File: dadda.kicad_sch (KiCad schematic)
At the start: 0 parts

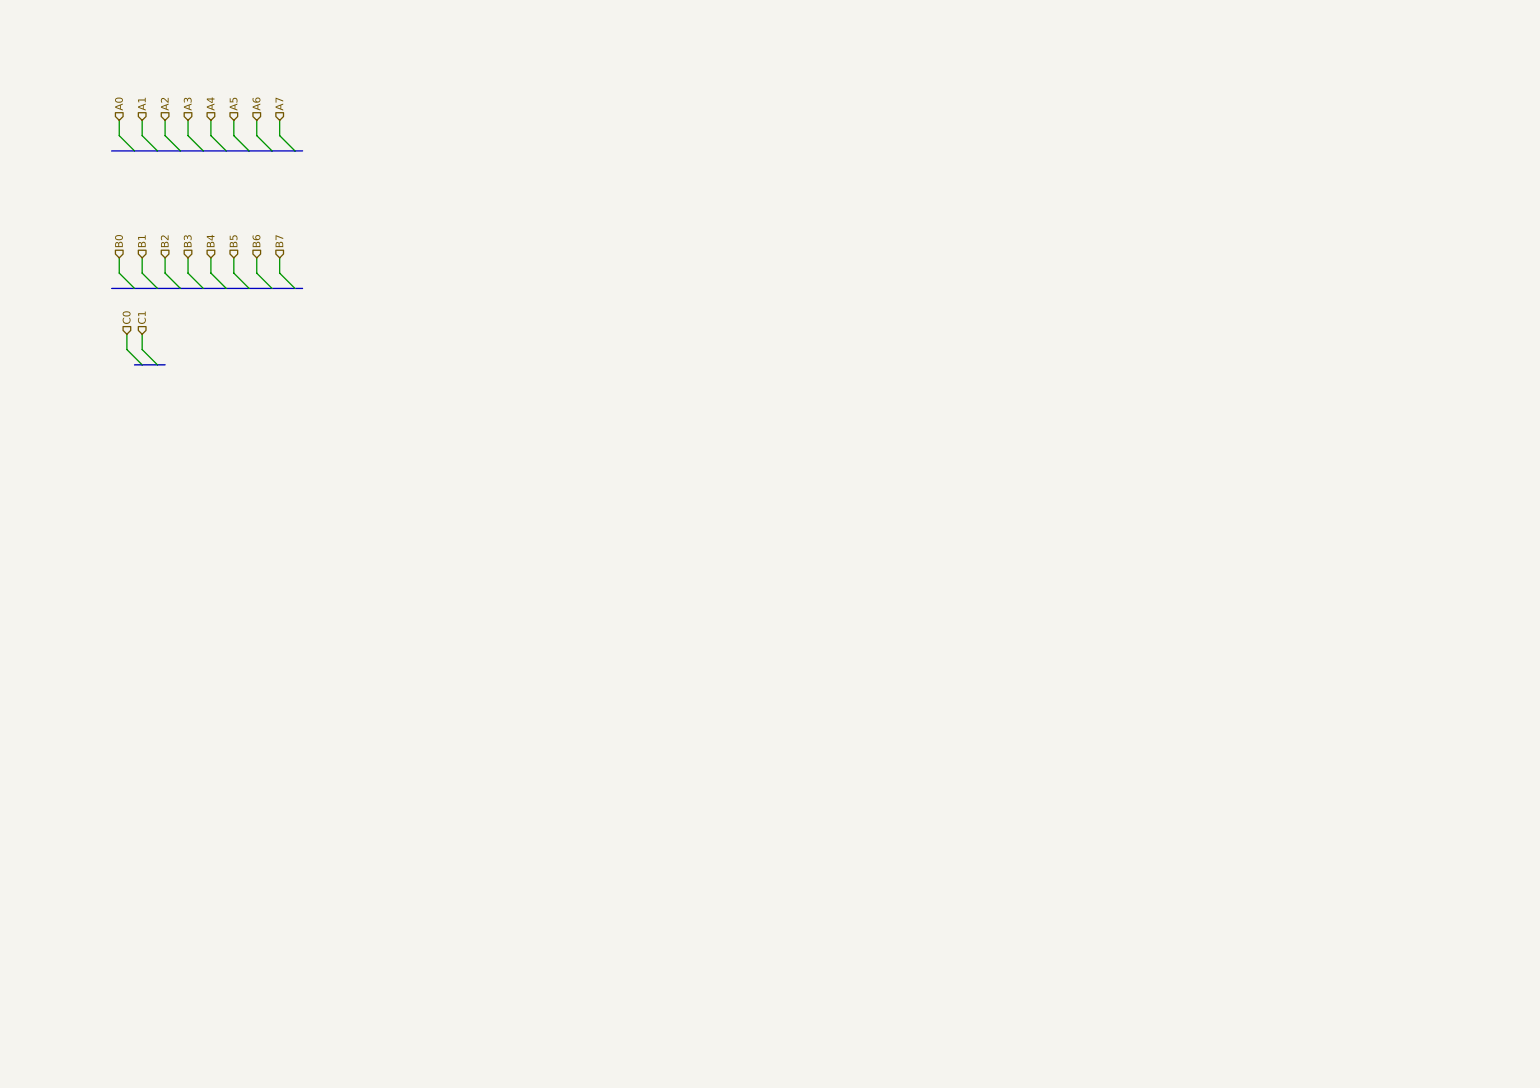
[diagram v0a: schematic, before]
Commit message: Added hierarchal partial product outputs, need to complete treemultiplier
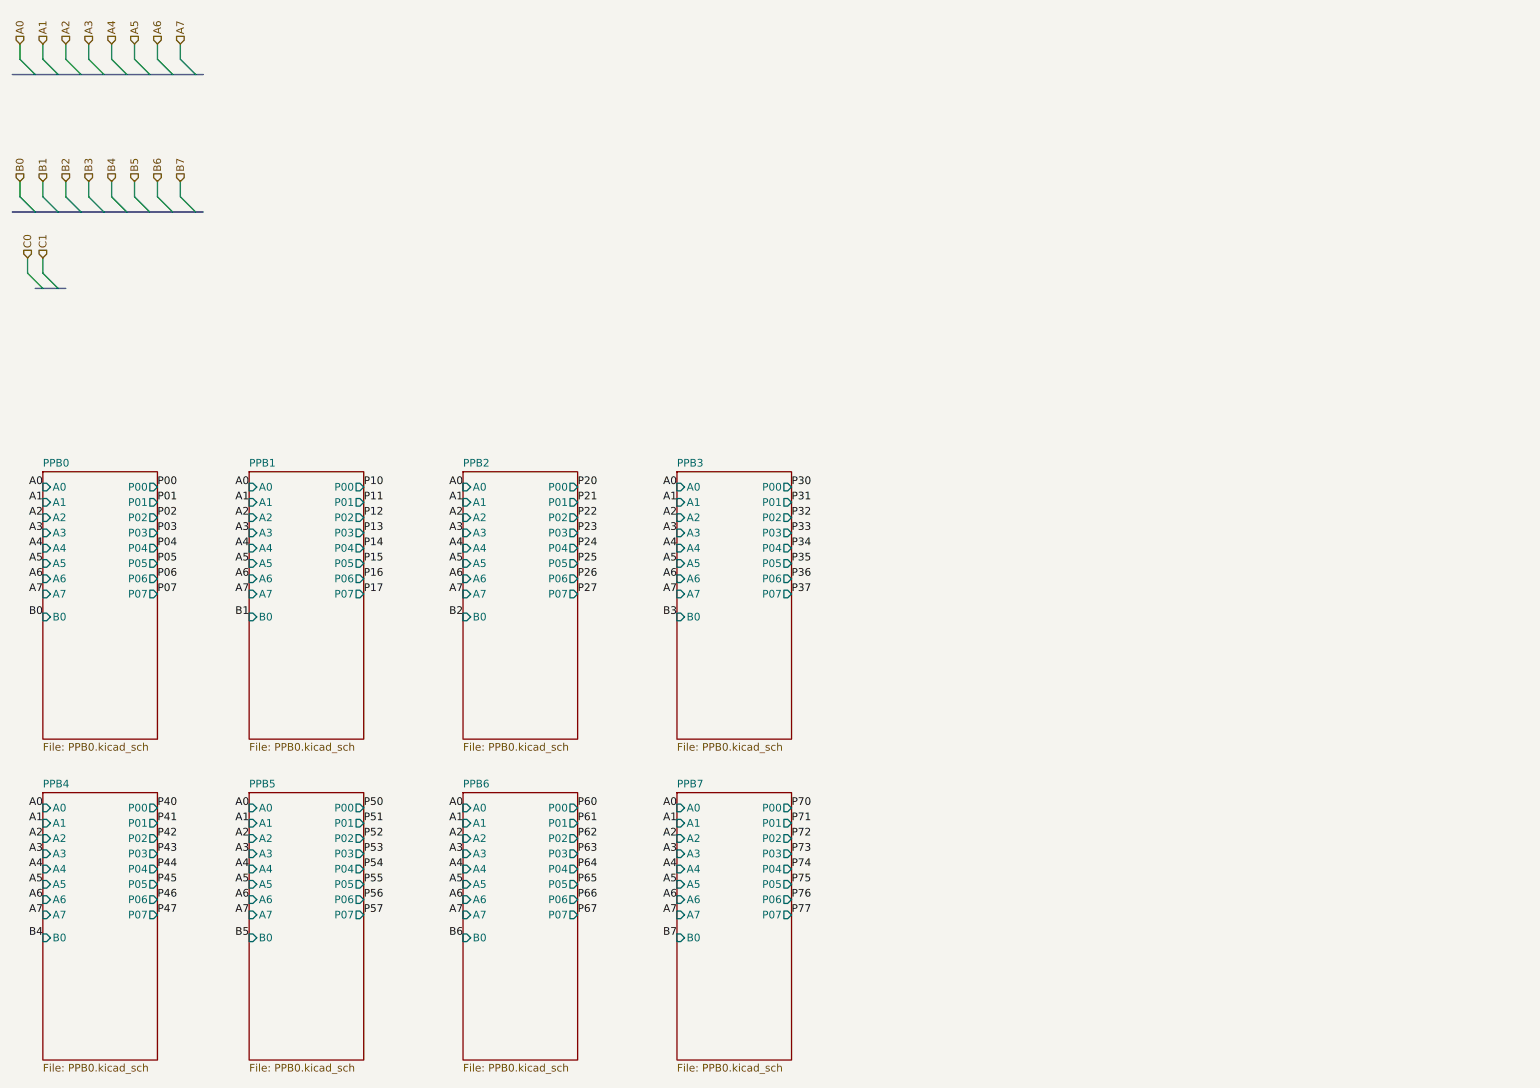
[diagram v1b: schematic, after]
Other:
- added sheet PPB0 (PPB0.kicad_sch)
- added sheet PPB1 (PPB0.kicad_sch)
- added sheet PPB2 (PPB0.kicad_sch)
- added sheet PPB3 (PPB0.kicad_sch)
- added sheet PPB4 (PPB0.kicad_sch)
- added sheet PPB5 (PPB0.kicad_sch)
- added sheet PPB6 (PPB0.kicad_sch)
- added sheet PPB7 (PPB0.kicad_sch)

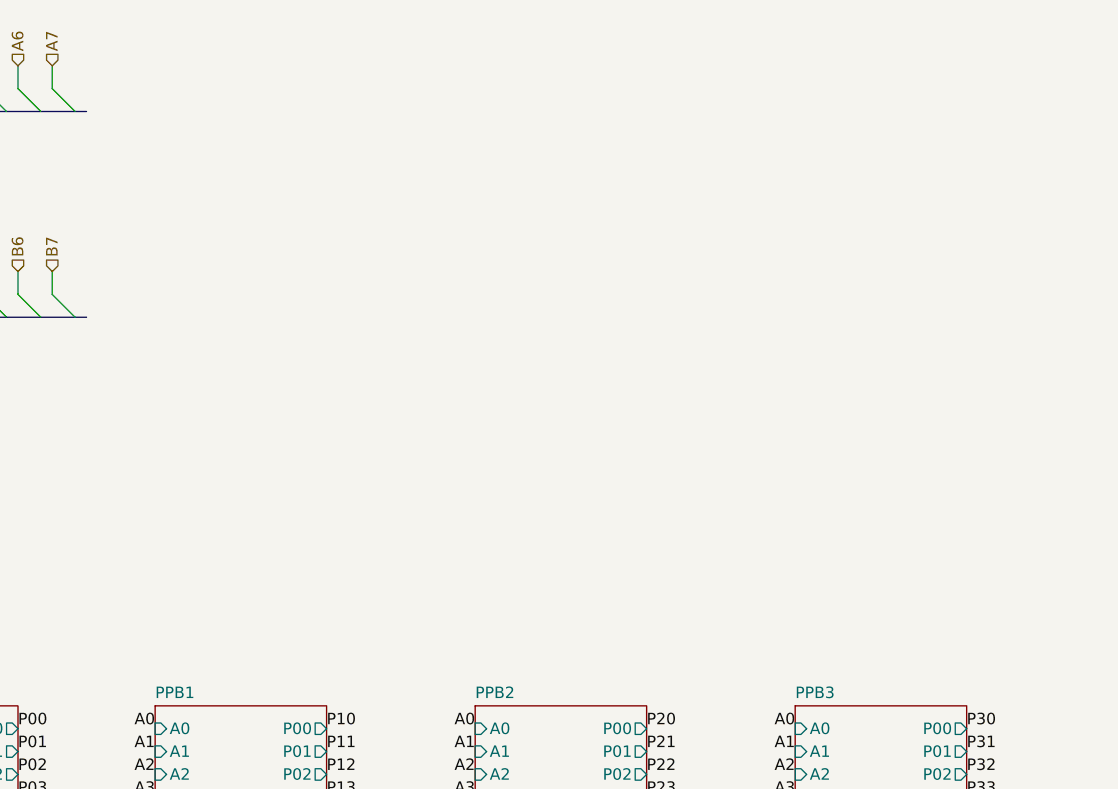
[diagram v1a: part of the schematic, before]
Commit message: Added first set of condensing adders, down to 4 rows total of Partials to add
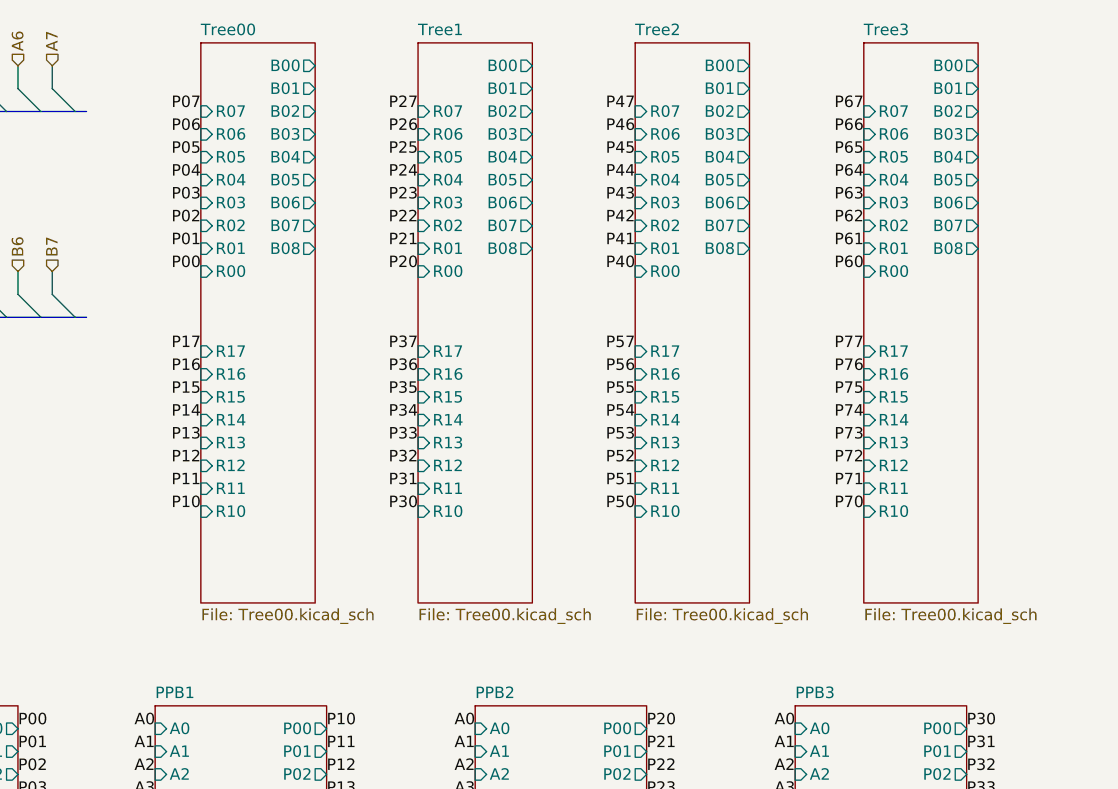
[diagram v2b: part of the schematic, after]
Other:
- added sheet Tree00 (Tree00.kicad_sch)
- added sheet Tree1 (Tree00.kicad_sch)
- added sheet Tree2 (Tree00.kicad_sch)
- added sheet Tree3 (Tree00.kicad_sch)

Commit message: Finished schematic, need to look at power output of the mux potentially to drive LED pins, otherwise logic SHOULD be done
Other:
- added sheet FinalTree (FinalTree.kicad_sch)
- added sheet Tree01 (Tree01.kicad_sch)
- added sheet Tree4 (Tree01.kicad_sch)
- sheet Tree00 ports: added B09; removed none
- sheet Tree1 ports: added B09; removed none
- sheet Tree2 ports: added B09; removed none
- sheet Tree3 ports: added B09; removed none

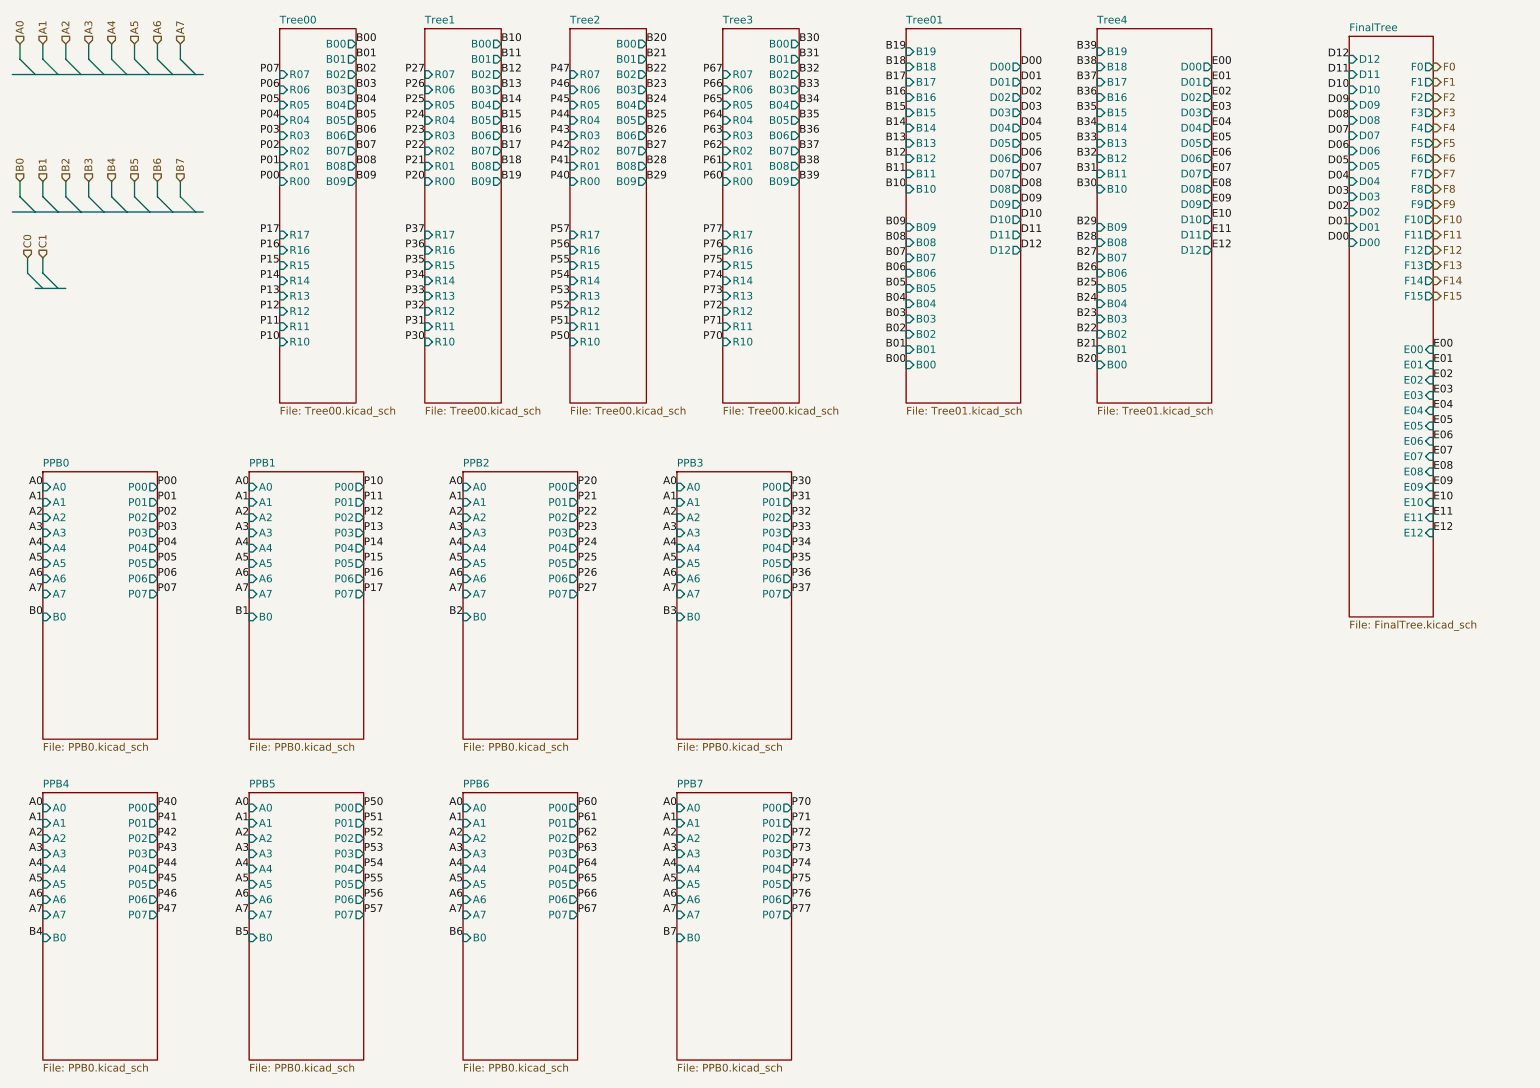
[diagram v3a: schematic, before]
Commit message: Fixed ERC issues and applied Footprints
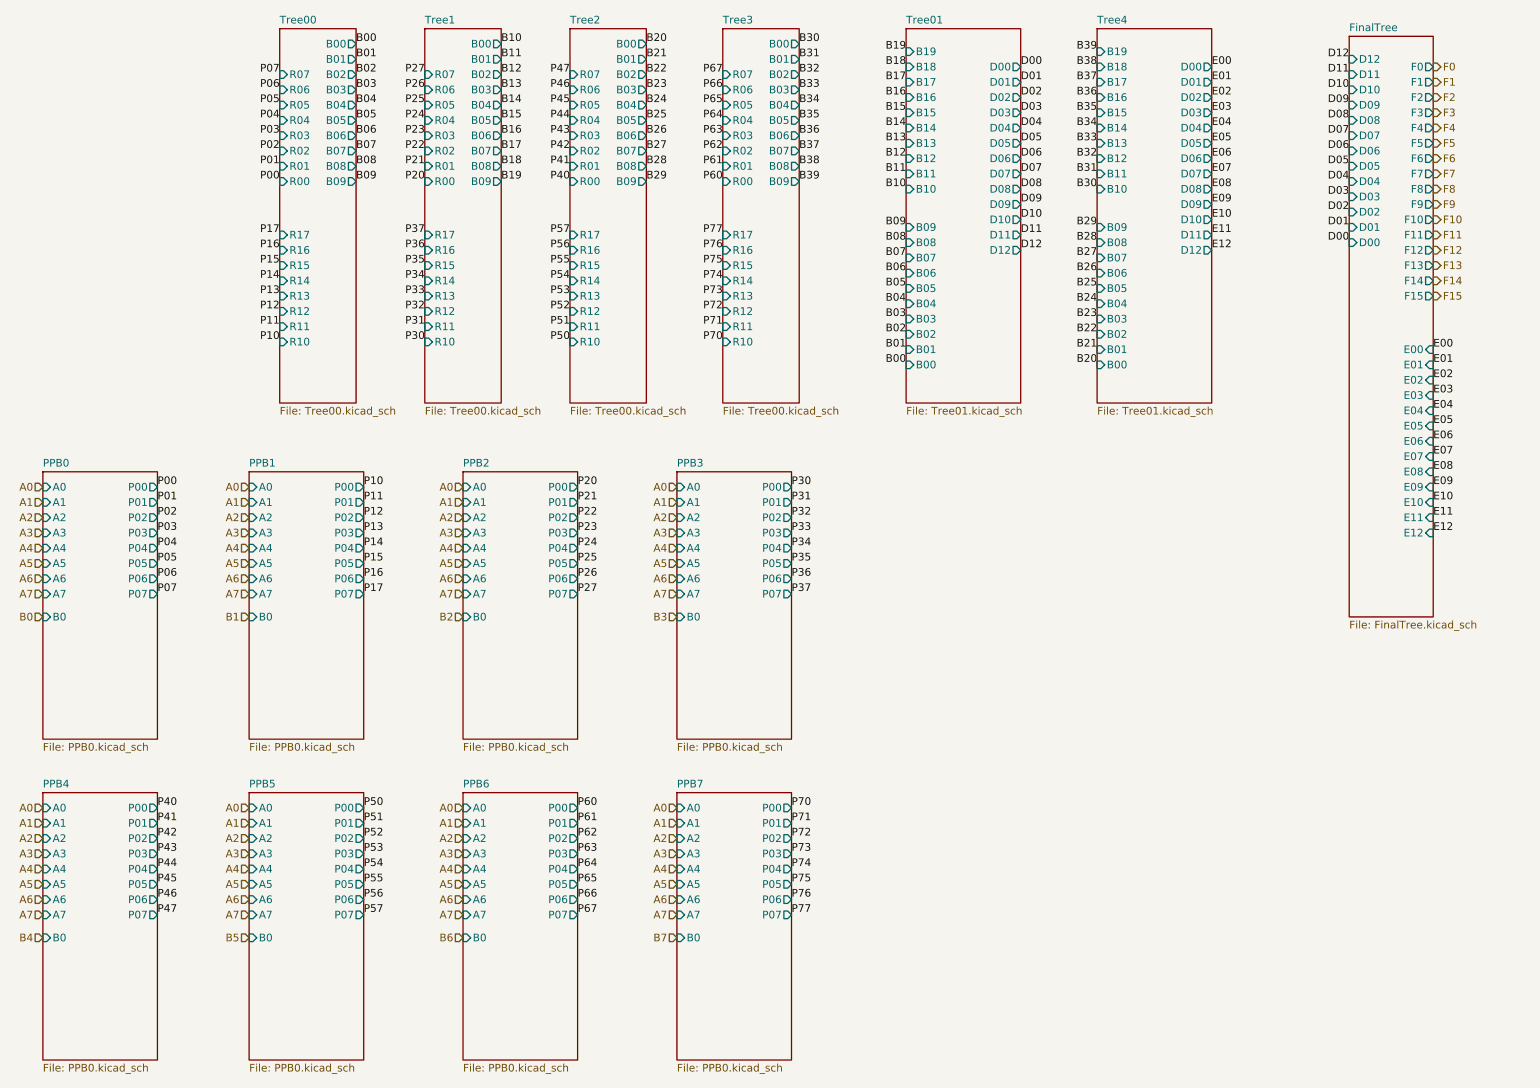
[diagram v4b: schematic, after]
